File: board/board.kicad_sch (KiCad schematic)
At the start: 2 parts, among them J1 013_PoE_rectified, J2 003_power

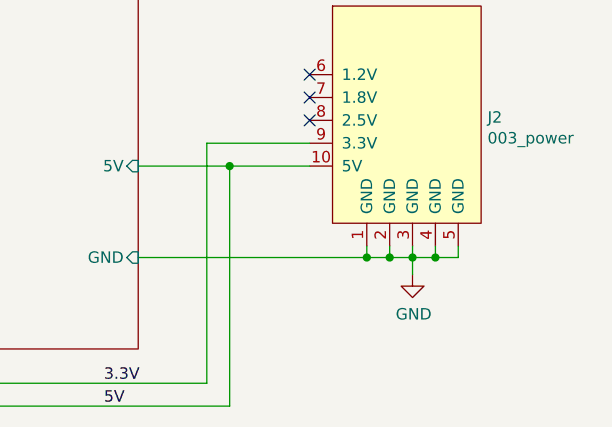
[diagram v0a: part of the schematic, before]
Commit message: improved thermal properties of layout
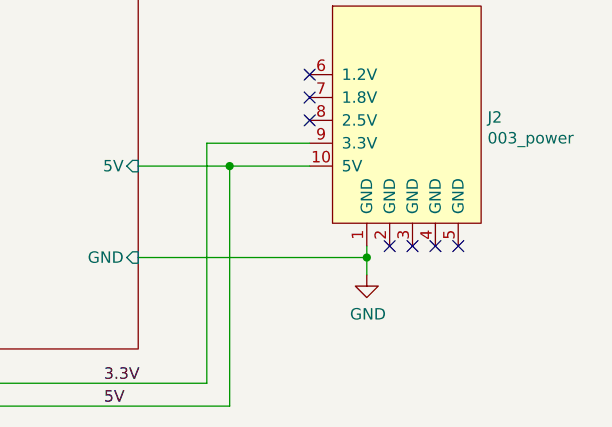
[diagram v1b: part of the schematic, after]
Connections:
- net GND: no longer J2.2 (GND), J2.3 (GND), J2.4 (GND), J2.5 (GND)
- no-connect marks 3 -> 7
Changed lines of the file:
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@@
 (kicad_sch (version 20211123) (generator eeschema)
   (paper "A4")
-  (junction (at 184.15 96.52) (diameter 0) (color 0 0 0 0)
-  )
-  (junction (at 186.69 96.52) (diameter 0) (color 0 0 0 0)
-  )
   (junction (at 163.83 86.36) (diameter 0) (color 0 0 0 0)
   )
   (junction (at 179.07 96.52) (diameter 0) (color 0 0 0 0)
   )
-  (junction (at 181.61 96.52) (diameter 0) (color 0 0 0 0)
-  )
   (junction (at 99.06 77.47) (diameter 0) (color 0 0 0 0)
   )
@@
   )
   (no_connect (at 172.72 78.74))
+  (no_connect (at 181.61 95.25))
+  (no_connect (at 184.15 95.25))
+  (no_connect (at 186.69 95.25))
+  (no_connect (at 189.23 95.25))
   (no_connect (at 172.72 81.28))
   (no_connect (at 172.72 76.2))
@@
     (stroke (width 0) (type default) (color 0 0 0 0))
   )
-  (wire (pts (xy 186.69 96.52) (xy 189.23 96.52))
-    (stroke (width 0) (type default) (color 0 0 0 0))
-  )
   (wire (pts (xy 97.79 85.09) (xy 99.06 85.09))
     (stroke (width 0) (type default) (color 0 0 0 0))
   )
-  (wire (pts (xy 181.61 96.52) (xy 184.15 96.52))
-    (stroke (width 0) (type default) (color 0 0 0 0))
-  )
   (wire (pts (xy 97.79 80.01) (xy 99.06 80.01))
     (stroke (width 0) (type default) (color 0 0 0 0))
@@
     (stroke (width 0) (type default) (color 0 0 0 0))
   )
-  (wire (pts (xy 189.23 96.52) (xy 189.23 95.25))
-    (stroke (width 0) (type default) (color 0 0 0 0))
-  )
-  (wire (pts (xy 184.15 95.25) (xy 184.15 96.52))
-    (stroke (width 0) (type default) (color 0 0 0 0))
-  )
   (wire (pts (xy 161.29 110.49) (xy 161.29 83.82))
     (stroke (width 0) (type default) (color 0 0 0 0))
@@
     (stroke (width 0) (type default) (color 0 0 0 0))
   )
-  (wire (pts (xy 181.61 96.52) (xy 179.07 96.52))
-    (stroke (width 0) (type default) (color 0 0 0 0))
-  )
-  (wire (pts (xy 186.69 96.52) (xy 186.69 95.25))
-    (stroke (width 0) (type default) (color 0 0 0 0))
-  )
   (wire (pts (xy 97.79 77.47) (xy 99.06 77.47))
     (stroke (width 0) (type default) (color 0 0 0 0))
@@
     (stroke (width 0) (type default) (color 0 0 0 0))
   )
-  (wire (pts (xy 181.61 95.25) (xy 181.61 96.52))
-    (stroke (width 0) (type default) (color 0 0 0 0))
-  )
   (wire (pts (xy 99.06 80.01) (xy 99.06 77.47))
     (stroke (width 0) (type default) (color 0 0 0 0))
@@
     (stroke (width 0) (type default) (color 0 0 0 0))
   )
-  (wire (pts (xy 184.15 96.52) (xy 186.69 96.52))
-    (stroke (width 0) (type default) (color 0 0 0 0))
-  )
-  (wire (pts (xy 184.15 98.425) (xy 184.15 96.52))
+  (wire (pts (xy 179.07 98.425) (xy 179.07 96.52))
     (stroke (width 0) (type default) (color 0 0 0 0))
   )
@@
     (pin "9")
   )
-  (symbol (lib_id "power:GND") (at 184.15 98.425 0) (unit 1)
-    (in_bom yes) (on_board yes)
-    (property "Reference" "#PWR0103" (id 0) (at 184.15 104.775 0)
-      (effects (font (size 1.27 1.27)) hide)
-    )
-    (property "Value" "GND" (id 1) (at 184.277 102.8192 0))
-    (property "Footprint" "" (id 2) (at 184.15 98.425 0)
-      (effects (font (size 1.27 1.27)) hide)
-    )
-    (property "Datasheet" "" (id 3) (at 184.15 98.425 0)
+  (symbol (lib_id "power:GND") (at 179.07 98.425 0) (unit 1)
+    (in_bom yes) (on_board yes)
+    (property "Reference" "#PWR0103" (id 0) (at 179.07 104.775 0)
+      (effects (font (size 1.27 1.27)) hide)
+    )
+    (property "Value" "GND" (id 1) (at 179.197 102.8192 0))
+    (property "Footprint" "" (id 2) (at 179.07 98.425 0)
+      (effects (font (size 1.27 1.27)) hide)
+    )
+    (property "Datasheet" "" (id 3) (at 179.07 98.425 0)
       (effects (font (size 1.27 1.27)) hide)
     )
@@
       (reference "J2") (unit 1) (value "003_power") (footprint "on_edge:on_edge_2x05_host")
     )
-    (path "/00000000-0000-0000-0000-00006083c3a8/3f193c86-a76f-4831-8da3-38c37ef79f23"
-      (reference "L1") (unit 1) (value "0R") (footprint "Inductor_SMD:L_1812_4532Metric")
-    )
     (path "/00000000-0000-0000-0000-00006083c3a8/4cede1f9-feab-4d64-94a8-4377200e4073"
-      (reference "R1") (unit 1) (value "2.2k") (footprint "Resistor_SMD:R_0603_1608Metric")
+      (reference "R1") (unit 1) (value "5.1k") (footprint "Resistor_SMD:R_0603_1608Metric")
     )
     (path "/00000000-0000-0000-0000-00006083c3a8/829fe45f-4f2a-494b-aa76-279476c8d8dc"
@@
     )
     (path "/00000000-0000-0000-0000-00006083c3a8/c2cd3993-73d9-41e5-b0f1-db67f319d603"
-      (reference "R6") (unit 1) (value "105k") (footprint "Resistor_SMD:R_0603_1608Metric")
+      (reference "R6") (unit 1) (value "110k") (footprint "Resistor_SMD:R_0603_1608Metric")
     )
     (path "/00000000-0000-0000-0000-00006083c3a8/18dc37b1-09ce-4dbd-b2fa-96b727679170"
